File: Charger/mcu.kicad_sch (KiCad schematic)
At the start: 2 parts, among them U23 RaspberryPi_Pico, U24 CD4051B

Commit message: Schematic trace update
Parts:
- added R72: 10k, symbol Device:R
- added U25: MCP6001-OT, Package_TO_SOT_SMD:SOT-23-5, symbol Amplifier_Operational:MCP6001-OT
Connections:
- net BAL_BalV6: now also U24.5 (X5)
- net BAL_BatV1: now also U24.13 (X0)
- net BAL_BatV2: now also U24.14 (X1)
- net BAL_BatV3: now also U24.15 (X2)
- net BAL_BatV4: now also U24.12 (X3)
- net BAL_BatV5: now also U24.1 (X4)
- net BAL_VBal: now also U23.9 (GPIO6)
- net ISENS_EN: now also U23.12 (GPIO9)
- net LOAD_EN: now also U23.10 (GPIO7)
- net LOAD_SetI: now also U23.11 (GPIO8)
- net PSU_Off: now also U23.4 (GPIO2), R72.2
- net PSU_OutV: now also U23.32 (GPIO27_ADC1)
- net PSU_SetI: now also U23.6 (GPIO4)
- net PSU_SetV: now also U23.5 (GPIO3)
- new net +3.3V: R72.1
- no-connect marks 2 -> 5
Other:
- note added: "Do zmiany po dobraniu multipleksera"

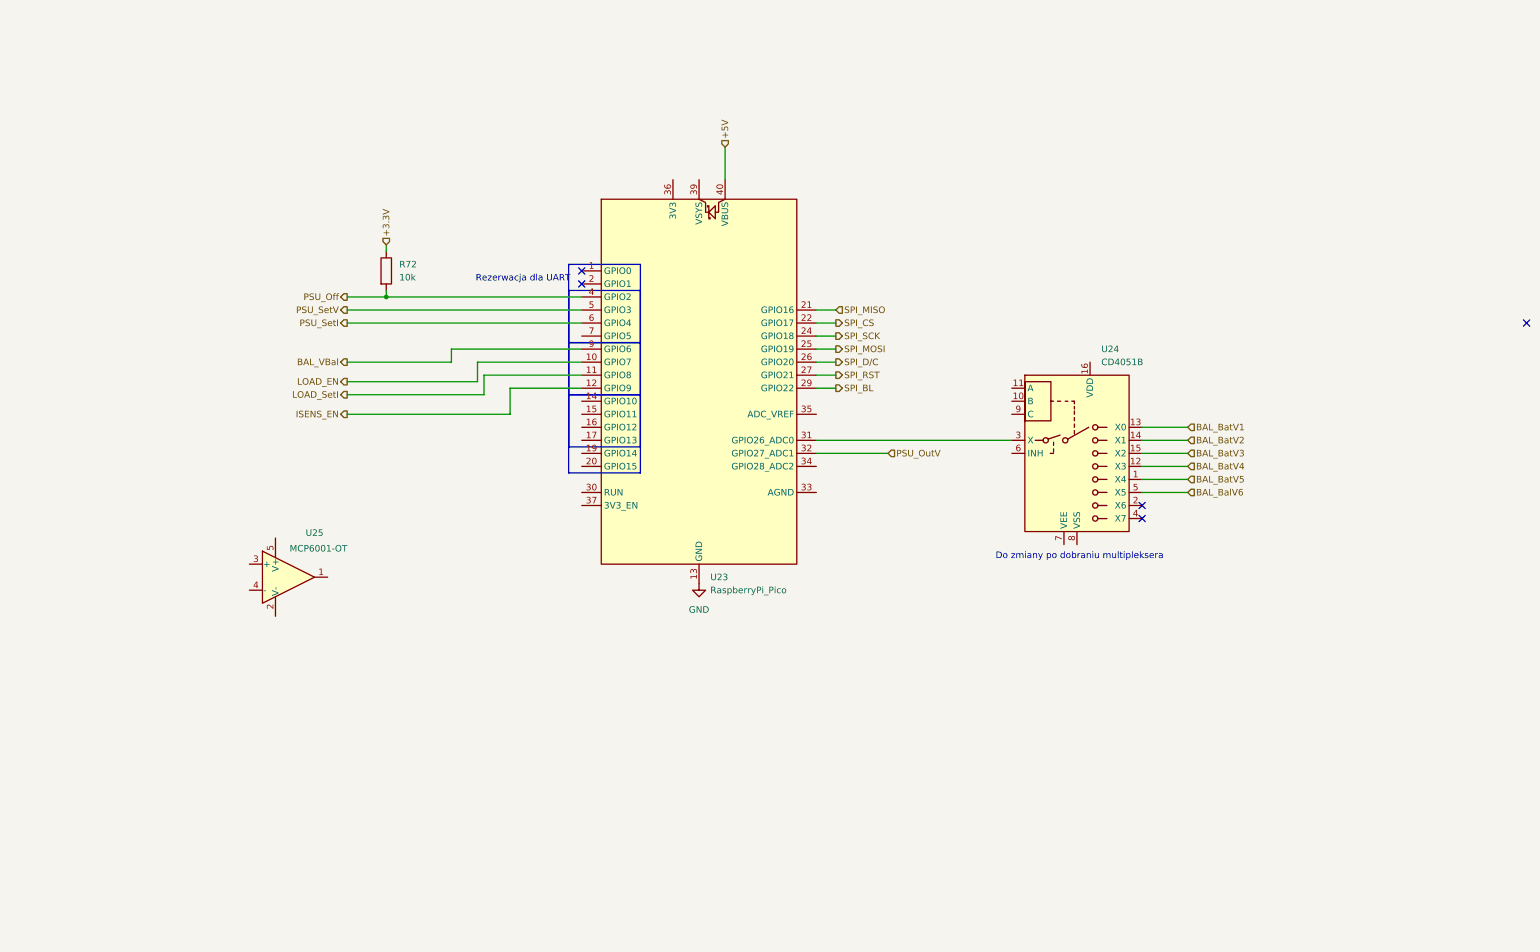
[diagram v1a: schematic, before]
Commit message: Semi finished pinning the mcu and added ui pins
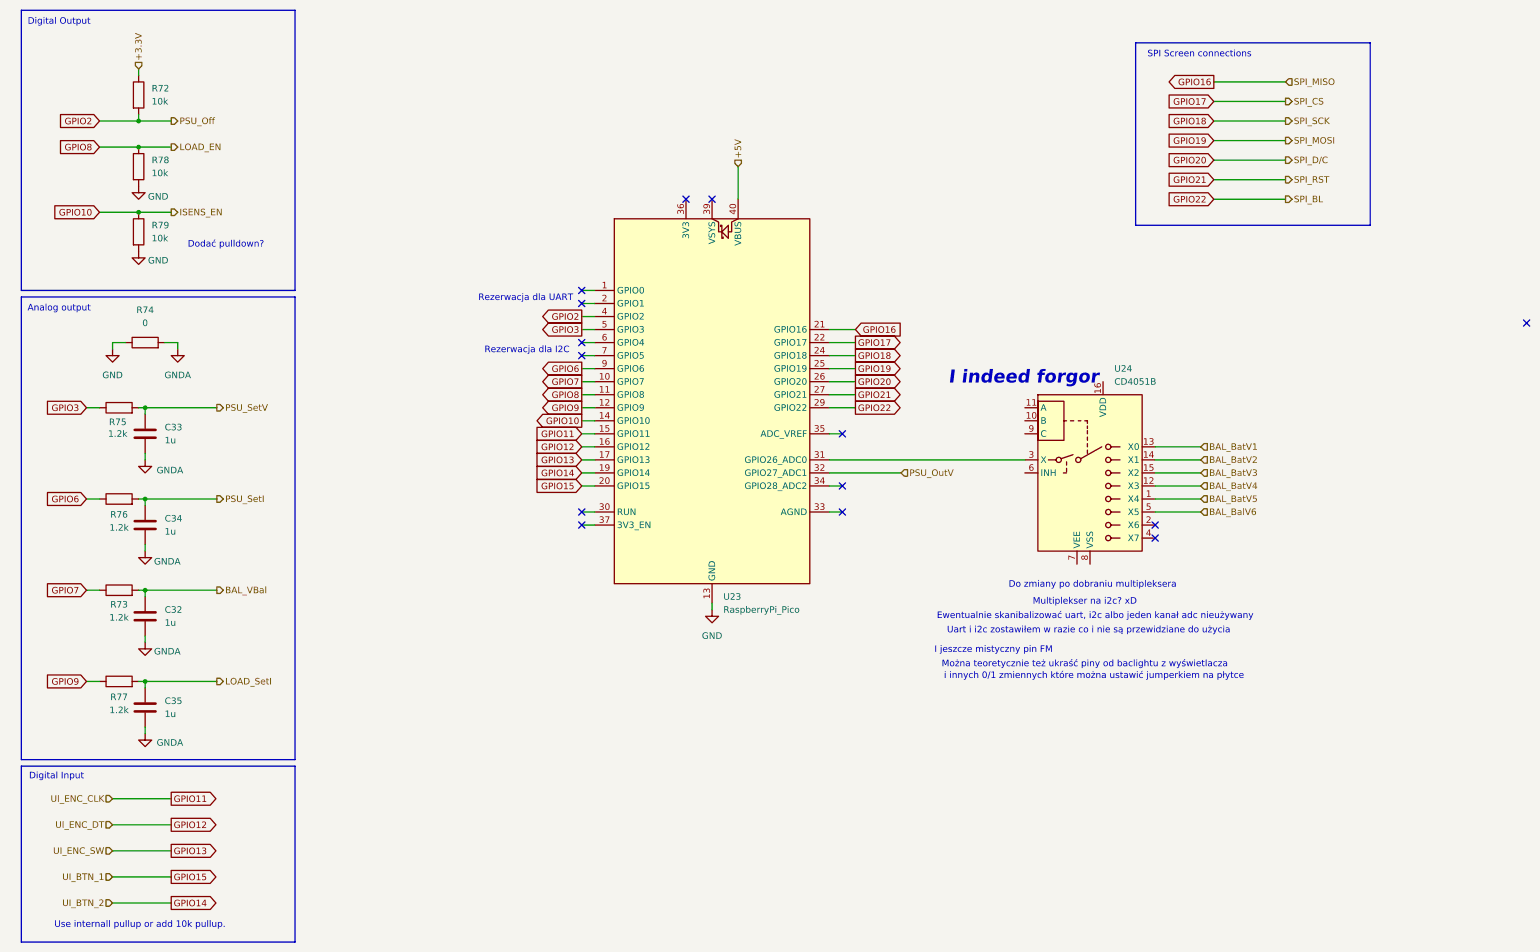
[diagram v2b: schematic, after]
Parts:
- removed U25: MCP6001-OT, Package_TO_SOT_SMD:SOT-23-5, symbol Amplifier_Operational:MCP6001-OT
- added C32, C33, C34, C35: 1u, symbol Device:C
- added R73, R75, R76, R77: 1.2k, symbol Device:R
- added R74: 0, symbol Device:R
- added R78, R79: 10k, symbol Device:R
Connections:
- net BAL_VBal: now also C32.1, R73.2; no longer U23.9 (GPIO6)
- net GND: now also R74.1, R78.2, R79.2
- net LOAD_SetI: now also C35.1, R77.2; no longer U23.11 (GPIO8)
- net PSU_SetI: now also C34.1, R76.2; no longer U23.6 (GPIO4)
- net PSU_SetV: now also C33.1, R75.2; no longer U23.5 (GPIO3)
- net GPIO10: now reaches U23.14 (GPIO10)
- net GPIO10: now also R79.1
- net GPIO11: now reaches U23.15 (GPIO11)
- net GPIO12: now reaches U23.16 (GPIO12)
- net GPIO13: now reaches U23.17 (GPIO13)
- net GPIO14: now reaches U23.19 (GPIO14)
- net GPIO15: now reaches U23.20 (GPIO15)
- net ISENS_EN renamed GPIO9
- net GPIO9: now also R77.1
- net LOAD_EN renamed GPIO7
- net GPIO7: now also R73.1
- net PSU_Off renamed GPIO2
- net SPI_BL renamed GPIO22
- net SPI_CS renamed GPIO17
- net SPI_D/C renamed GPIO20
- net SPI_MISO renamed GPIO16
- net SPI_MOSI renamed GPIO19
- net SPI_RST renamed GPIO21
- net SPI_SCK renamed GPIO18
- new net GNDA: C32.2, C33.2, C34.2, C35.2, R74.2
- new net GPIO3: R75.1, U23.5 (GPIO3)
- new net GPIO6: R76.1, U23.9 (GPIO6)
- new net GPIO8: R78.1, U23.11 (GPIO8)
- no-connect marks 5 -> 14
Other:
- note added: "Analog output"
- note added: "Digital Input"
- note added: "Digital Output"
- note added: "Dodać pulldown?"
- note added: "Ewentualnie skanibalizować uart, i2c albo jeden kanał adc nieużywany"
- note added: "I indeed forgor"
- note added: "I jeszcze mistyczny pin FM"
- note added: "Można teoretycznie też ukraść piny od baclightu z wyświetlacza"
- note added: "Multiplekser na i2c? xD"
- note added: "Rezerwacja dla I2C"
- note added: "SPI Screen connections"
- note added: "Uart i i2c zostawiłem w razie co i nie są przewidziane do użycia"
- note added: "Use internall pullup or add 10k pullup."
- note added: "i innych 0/1 zmiennych które można ustawić jumperkiem na płytce"
- moved on the sheet: R72, U23, U24

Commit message: przegląd
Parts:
- C32, C33, C34, C35: footprint (none) -> Capacitor_SMD:C_0805_2012Metric_Pad1.18x1.45mm_HandSolder
- R72, R73, R74, R75, R76, R77, R78, R79: footprint (none) -> Resistor_SMD:R_0805_2012Metric_Pad1.20x1.40mm_HandSolder
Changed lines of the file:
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@@
 			)
 		)
-		(property "Footprint" ""
+		(property "Footprint" "Resistor_SMD:R_0805_2012Metric_Pad1.20x1.40mm_HandSolder"
 			(at 38.1 80.518 90)
 			(effects
@@
 			)
 		)
-		(property "Footprint" ""
+		(property "Footprint" "Capacitor_SMD:C_0805_2012Metric_Pad1.18x1.45mm_HandSolder"
 			(at 39.0652 118.11 0)
 			(effects
@@
 			)
 		)
-		(property "Footprint" ""
+		(property "Footprint" "Capacitor_SMD:C_0805_2012Metric_Pad1.18x1.45mm_HandSolder"
 			(at 39.0652 100.33 0)
 			(effects
@@
 			)
 		)
-		(property "Footprint" ""
+		(property "Footprint" "Resistor_SMD:R_0805_2012Metric_Pad1.20x1.40mm_HandSolder"
 			(at 33.02 93.218 90)
 			(effects
@@
 			)
 		)
-		(property "Footprint" ""
+		(property "Footprint" "Capacitor_SMD:C_0805_2012Metric_Pad1.18x1.45mm_HandSolder"
 			(at 39.0652 153.67 0)
 			(effects
@@
 			)
 		)
-		(property "Footprint" ""
+		(property "Footprint" "Resistor_SMD:R_0805_2012Metric_Pad1.20x1.40mm_HandSolder"
 			(at 35.052 57.15 90)
 			(effects
@@
 			)
 		)
-		(property "Footprint" ""
+		(property "Footprint" "Resistor_SMD:R_0805_2012Metric_Pad1.20x1.40mm_HandSolder"
 			(at 33.02 146.558 90)
 			(effects
@@
 			)
 		)
-		(property "Footprint" ""
+		(property "Footprint" "Resistor_SMD:R_0805_2012Metric_Pad1.20x1.40mm_HandSolder"
 			(at 35.052 44.45 90)
 			(effects
@@
 			)
 		)
-		(property "Footprint" ""
+		(property "Footprint" "Resistor_SMD:R_0805_2012Metric_Pad1.20x1.40mm_HandSolder"
 			(at 35.052 30.48 90)
 			(effects
@@
 			)
 		)
-		(property "Footprint" ""
+		(property "Footprint" "Resistor_SMD:R_0805_2012Metric_Pad1.20x1.40mm_HandSolder"
 			(at 33.02 128.778 90)
 			(effects
@@
 			)
 		)
-		(property "Footprint" ""
+		(property "Footprint" "Capacitor_SMD:C_0805_2012Metric_Pad1.18x1.45mm_HandSolder"
 			(at 39.0652 135.89 0)
 			(effects
@@
 			)
 		)
-		(property "Footprint" ""
+		(property "Footprint" "Resistor_SMD:R_0805_2012Metric_Pad1.20x1.40mm_HandSolder"
 			(at 33.02 110.998 90)
 			(effects

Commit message: Notes after design meeting
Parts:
- added C36, C37, C38, C39: 100n, symbol Device:C
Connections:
- net +5V: now also C36.1
- net GND: now also C36.2, C37.2, C38.2, C39.2
- net GNDA: now also U23.33 (AGND)
- no-connect marks 14 -> 10
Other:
- note added: "1 pin na 1 wire"
- note added: "BL na zworce"
- note added: "Krótkie linie Digital"
- note added: "jumoerek"
- note added: "na multiplekser"
- note added: "pomiar i"
- note removed: "Do zmiany po dobraniu multipleksera"
- note removed: "Dodać pulldown?"
- note removed: "Multiplekser na i2c? xD"
- note removed: "Rezerwacja dla I2C"

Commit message: UPDATE UC
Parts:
- removed C38, C39: 100n, symbol Device:C
- added J6: 1/0_Select_Conn, Connector_PinHeader_2.54mm:PinHeader_1x03_P2.54mm_Vertical, symbol Connector:Conn_01x03_Pin
- C36, C37: footprint (none) -> Capacitor_SMD:C_0805_2012Metric_Pad1.18x1.45mm_HandSolder
- U23: footprint Module_RaspberryPi_Pico:RaspberryPi_Pico_Common -> Module_RaspberryPi_Pico:RaspberryPi_Pico_Common_SMD
- U24: footprint (none) -> Package_SO:SO-16_5.3x10.2mm_P1.27mm
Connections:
- net +3.3V: now also C37.1, U24.16 (VDD), J6.1 (Pin_1)
- net +5V: now also U23.39 (VSYS); no longer U23.40 (VBUS)
- net GND: now also U24.6 (INH), U24.8 (VSS), J6.3 (Pin_3)
- net GNDA: now also U24.7 (VEE)
- net GPIO22: now also U24.11 (A)
- net PSU_OutV: now also U24.2 (X6); no longer U23.32 (GPIO27_ADC1)
- net GPIO27: now reaches U24.10 (B)
- net GPIO27: now also U23.32 (GPIO27_ADC1)
- net ADC_0: now reaches U23.31 (GPIO26_ADC0), U24.3 (X)
- net PSU_OutI: now reaches U24.4 (X7)
- net GPIO28: now reaches U24.9 (C)
- net GPIO28: now also U23.34 (GPIO28_ADC2)
- net GPIO4: now reaches U23.6 (GPIO4)
- new net SPI_BL: J6.2 (Pin_2)
- no-connect marks 10 -> 8
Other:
- note added: "Use internall pullup or add 10k pullup. Add debounce circuit"
- note added: "czy to konieczne?"
- note removed: "1 pin na 1 wire"
- note removed: "Ewentualnie skanibalizować uart, i2c albo jeden kanał adc nieużywany"
- note removed: "I indeed forgor"
- note removed: "Można teoretycznie też ukraść piny od baclightu z wyświetlacza"
- note removed: "Uart i i2c zostawiłem w razie co i nie są przewidziane do użycia"
- note removed: "Use internall pullup or add 10k pullup."
- note removed: "i innych 0/1 zmiennych które można ustawić jumperkiem na płytce"
- note removed: "na multiplekser"
- note removed: "pomiar i"
- moved on the sheet: C36, C37, R72, R78, R79, U24

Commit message: pcb up
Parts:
- removed R74: 0, Resistor_SMD:R_0805_2012Metric_Pad1.20x1.40mm_HandSolder, symbol Device:R
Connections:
- net GNDA is gone; now on net GND: C32.2, C33.2, C34.2, C35.2, U23.33 (AGND), U24.7 (VEE)
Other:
- note added: "dalem jedna mase"

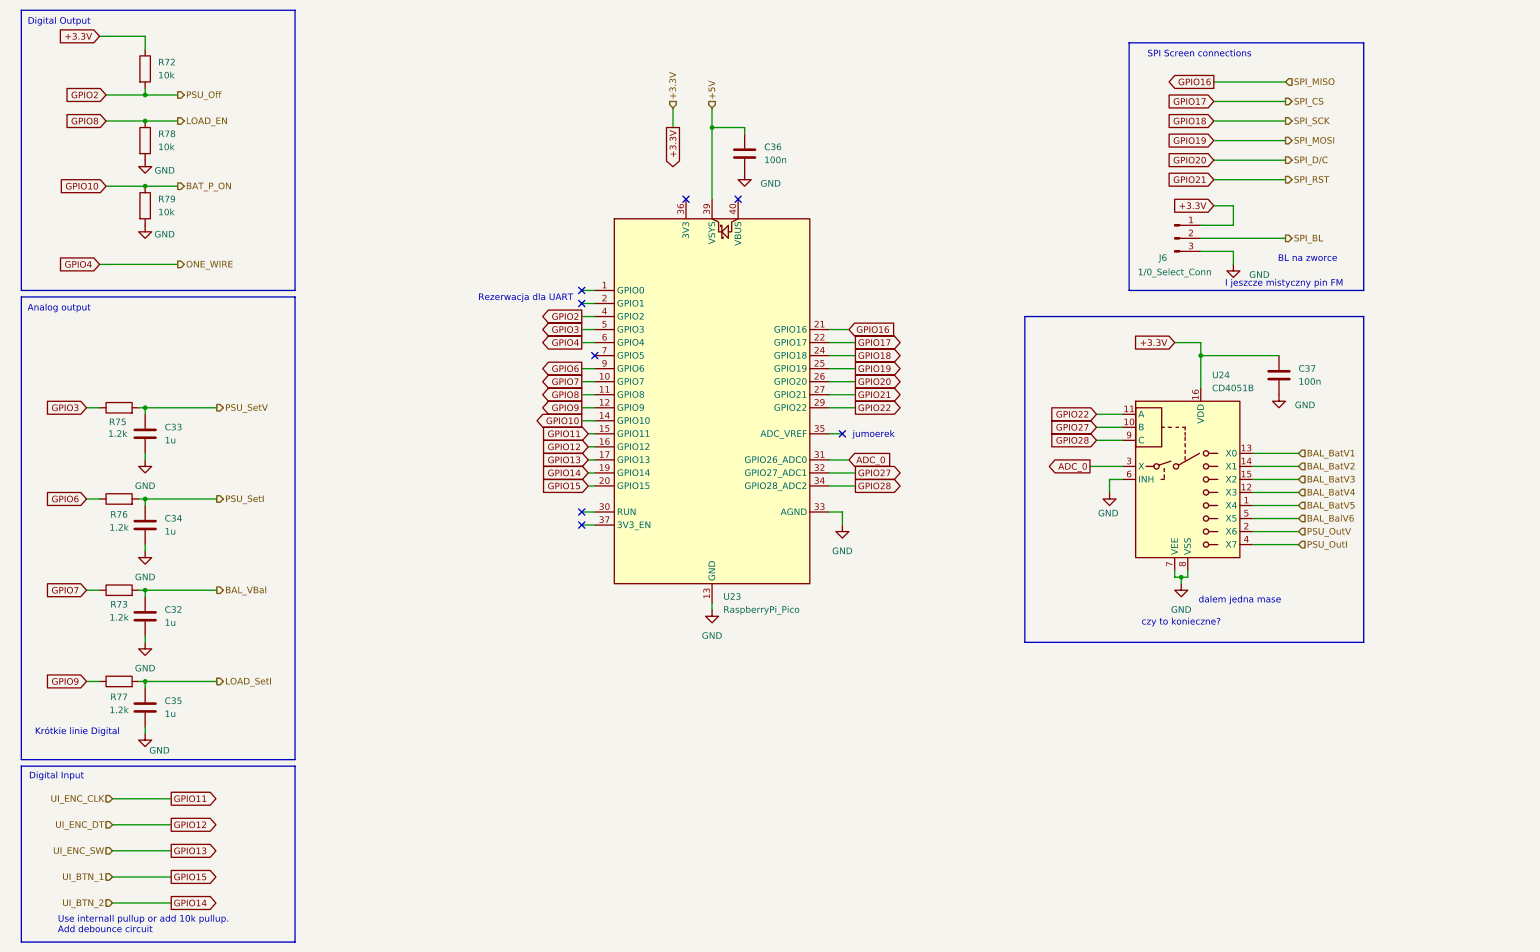
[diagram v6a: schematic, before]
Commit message: Changed SPI connector and MUX pins
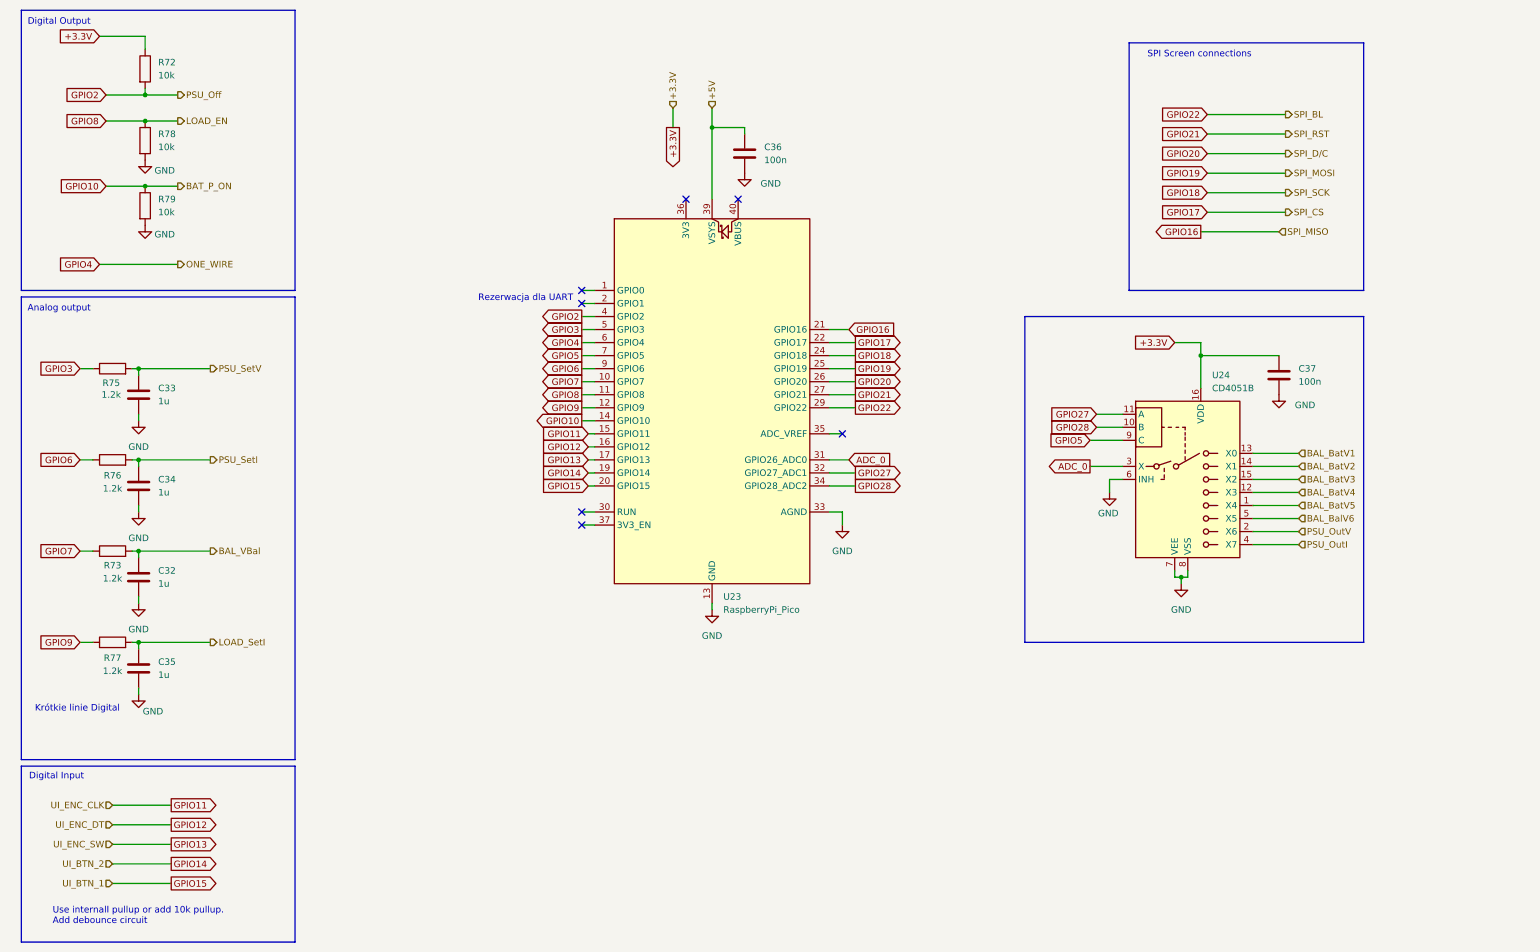
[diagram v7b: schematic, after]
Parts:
- removed J6: 1/0_Select_Conn, Connector_PinHeader_2.54mm:PinHeader_1x03_P2.54mm_Vertical, symbol Connector:Conn_01x03_Pin
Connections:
- net GPIO22: no longer U24.11 (A)
- net GPIO27: now also U24.11 (A); no longer U24.10 (B)
- net GPIO28: now also U24.10 (B); no longer U24.9 (C)
- net GPIO5: now reaches U23.7 (GPIO5)
- net GPIO5: now also U24.9 (C)
- no-connect marks 8 -> 7
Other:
- note removed: "BL na zworce"
- note removed: "I jeszcze mistyczny pin FM"
- note removed: "czy to konieczne?"
- note removed: "dalem jedna mase"
- note removed: "jumoerek"
- moved on the sheet: C32, C33, C34, C35, R73, R75, R76, R77

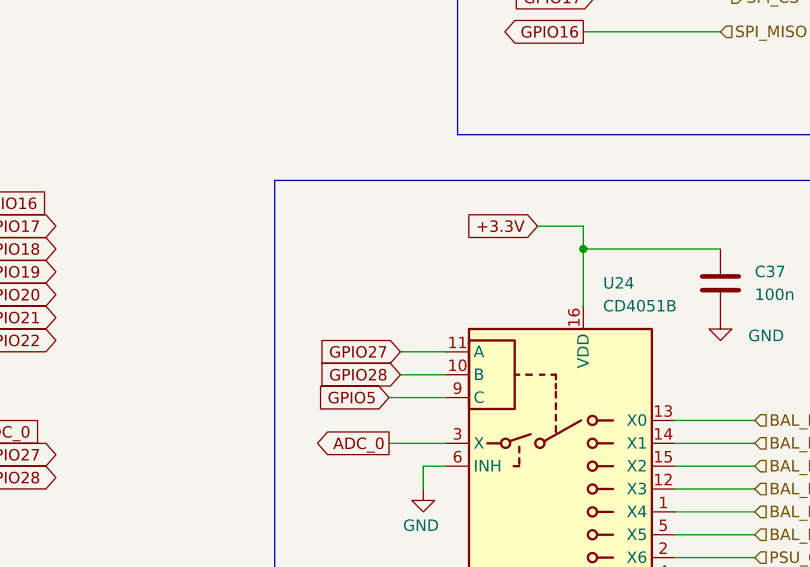
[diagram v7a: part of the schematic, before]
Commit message: Updated buy list with mcu components
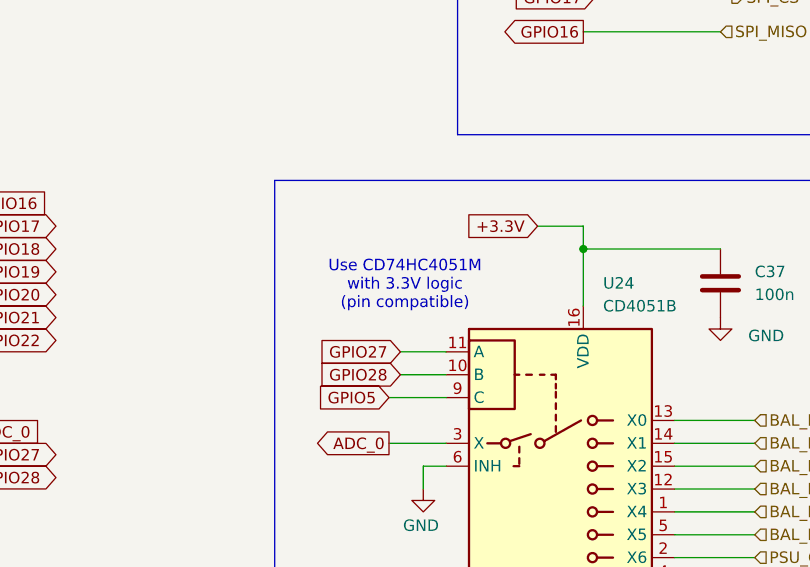
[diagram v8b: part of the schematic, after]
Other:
- note added: "Use CD74HC4051M with 3.3V logic (pin compatible)"
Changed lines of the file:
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@@
+		)
+	)
+	(text "Use CD74HC4051M \nwith 3.3V logic\n(pin compatible)"
+		(exclude_from_sim no)
+		(at 224.028 85.344 0)
+		(effects
+			(font
+				(size 1.27 1.27)
+			)
 		)
 	)
